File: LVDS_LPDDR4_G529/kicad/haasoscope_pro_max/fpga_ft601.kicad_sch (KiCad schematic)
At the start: 2 parts, among them U2 FT601Q_Aligned, U3 Ti90G529_Functions

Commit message: Aligned schematics, sort of
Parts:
- U3: footprint G529:BGA-529_23x23_19.0x19.0mm -> haasoscope_pro_adc_fpga_board:BGA-529_23x23_19.0x19.0mm
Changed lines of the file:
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@@
 			)
 		)
-		(property "Footprint" "G529:BGA-529_23x23_19.0x19.0mm"
+		(property "Footprint" "haasoscope_pro_adc_fpga_board:BGA-529_23x23_19.0x19.0mm"
 			(at 96.52 91.44 0)
 			(effects

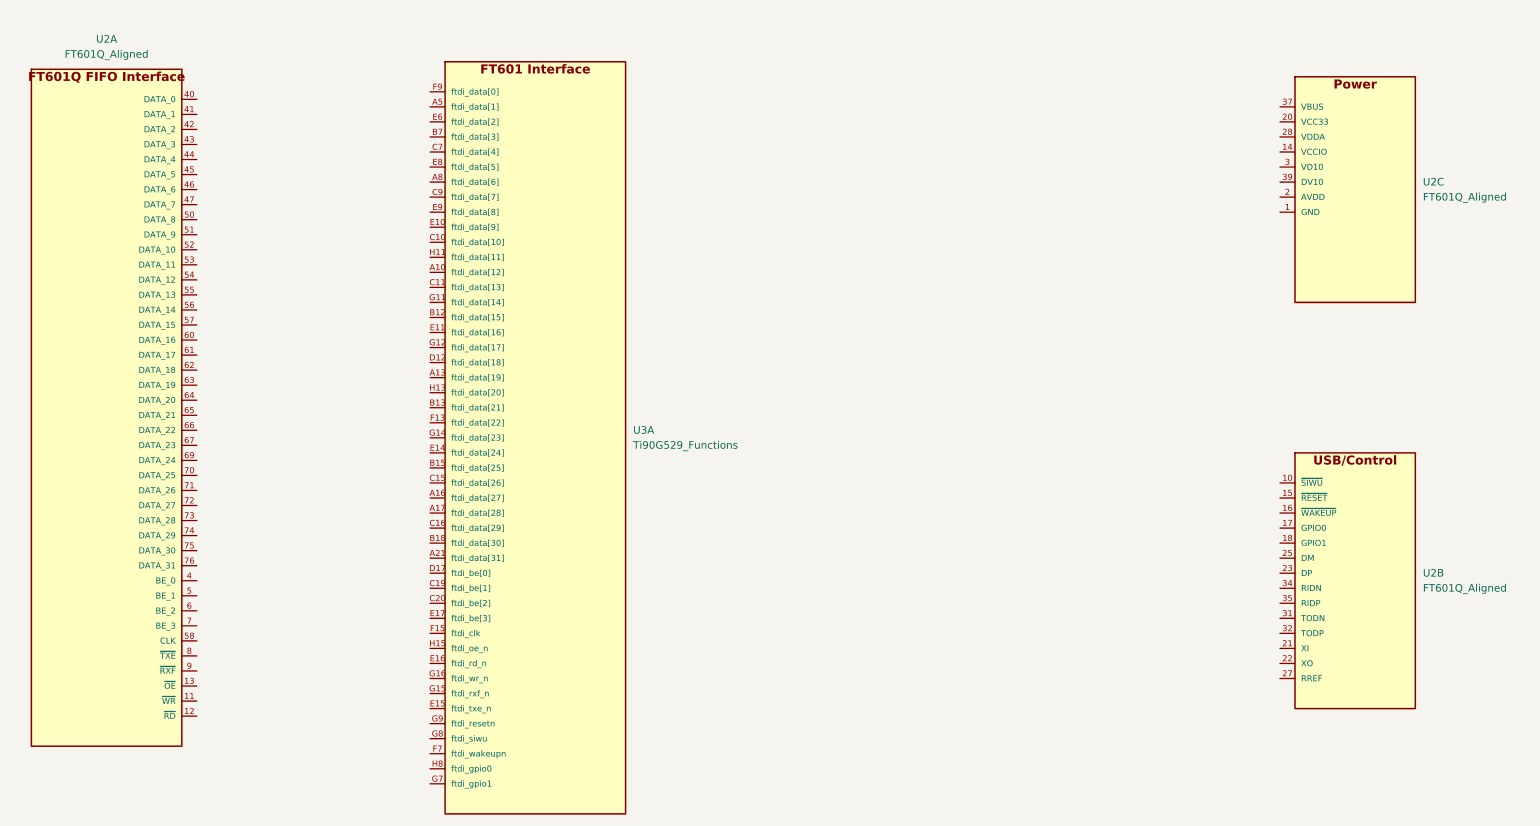
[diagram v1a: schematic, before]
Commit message: Aligned schematics, better
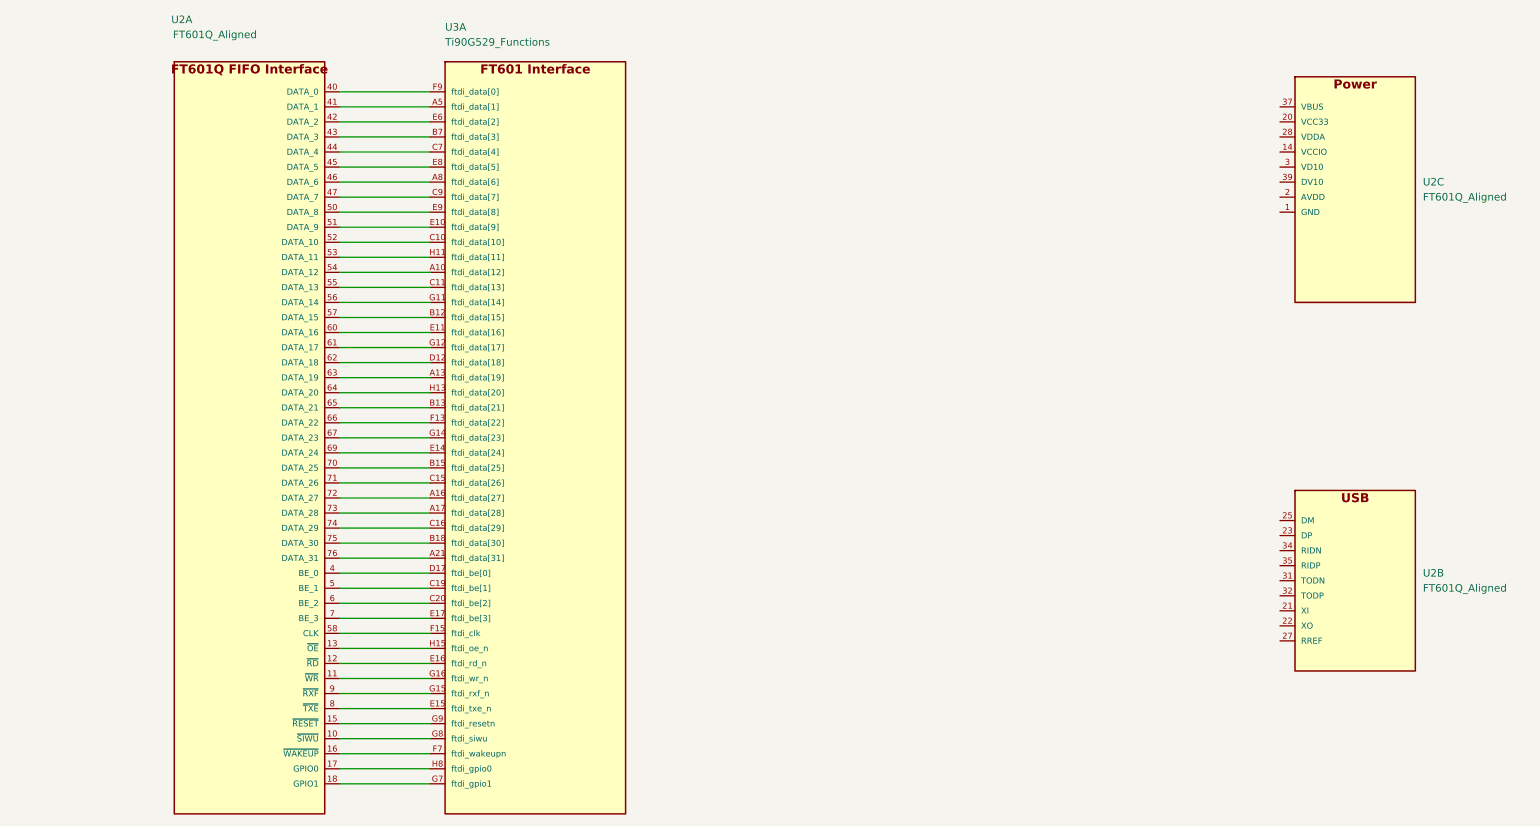
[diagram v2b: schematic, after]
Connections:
- net at U2.11 (~{WR}): now also U3.G16 (ftdi_wr_n)
- net at U2.12 (~{RD}): now also U3.E16 (ftdi_rd_n)
- net at U2.13 (~{OE}): now also U3.H15 (ftdi_oe_n)
- net at U2.4 (BE_0): now also U3.D17 (ftdi_be[0])
- net at U2.40 (DATA_0): now also U3.F9 (ftdi_data[0])
- net at U2.41 (DATA_1): now also U3.A5 (ftdi_data[1])
- net at U2.42 (DATA_2): now also U3.E6 (ftdi_data[2])
- net at U2.43 (DATA_3): now also U3.B7 (ftdi_data[3])
- net at U2.44 (DATA_4): now also U3.C7 (ftdi_data[4])
- net at U2.45 (DATA_5): now also U3.E8 (ftdi_data[5])
- net at U2.46 (DATA_6): now also U3.A8 (ftdi_data[6])
- net at U2.47 (DATA_7): now also U3.C9 (ftdi_data[7])
- net at U2.5 (BE_1): now also U3.C19 (ftdi_be[1])
- net at U2.50 (DATA_8): now also U3.E9 (ftdi_data[8])
- net at U2.51 (DATA_9): now also U3.E10 (ftdi_data[9])
- net at U2.52 (DATA_10): now also U3.C10 (ftdi_data[10])
- net at U2.53 (DATA_11): now also U3.H11 (ftdi_data[11])
- net at U2.54 (DATA_12): now also U3.A10 (ftdi_data[12])
- net at U2.55 (DATA_13): now also U3.C11 (ftdi_data[13])
- net at U2.56 (DATA_14): now also U3.G11 (ftdi_data[14])
- net at U2.57 (DATA_15): now also U3.B12 (ftdi_data[15])
- net at U2.58 (CLK): now also U3.F15 (ftdi_clk)
- net at U2.6 (BE_2): now also U3.C20 (ftdi_be[2])
- net at U2.60 (DATA_16): now also U3.E11 (ftdi_data[16])
- net at U2.61 (DATA_17): now also U3.G12 (ftdi_data[17])
- net at U2.62 (DATA_18): now also U3.D12 (ftdi_data[18])
- net at U2.63 (DATA_19): now also U3.A13 (ftdi_data[19])
- net at U2.64 (DATA_20): now also U3.H13 (ftdi_data[20])
- net at U2.65 (DATA_21): now also U3.B13 (ftdi_data[21])
- net at U2.66 (DATA_22): now also U3.F13 (ftdi_data[22])
- net at U2.67 (DATA_23): now also U3.G14 (ftdi_data[23])
- net at U2.69 (DATA_24): now also U3.E14 (ftdi_data[24])
- net at U2.7 (BE_3): now also U3.E17 (ftdi_be[3])
- net at U2.70 (DATA_25): now also U3.B15 (ftdi_data[25])
- net at U2.71 (DATA_26): now also U3.C15 (ftdi_data[26])
- net at U2.72 (DATA_27): now also U3.A16 (ftdi_data[27])
- net at U2.73 (DATA_28): now also U3.A17 (ftdi_data[28])
- net at U2.74 (DATA_29): now also U3.C16 (ftdi_data[29])
- net at U2.75 (DATA_30): now also U3.B18 (ftdi_data[30])
- net at U2.76 (DATA_31): now also U3.A21 (ftdi_data[31])
- net at U2.8 (~{TXE}): now also U3.E15 (ftdi_txe_n)
- net at U2.9 (~{RXF}): now also U3.G15 (ftdi_rxf_n)
- net at U3.F7 (ftdi_wakeupn): now also U2.16 (~{WAKEUP})
- net at U3.G7 (ftdi_gpio1): now also U2.18 (GPIO1)
- net at U3.G8 (ftdi_siwu): now also U2.10 (~{SIWU})
- net at U3.G9 (ftdi_resetn): now also U2.15 (~{RESET})
- net at U3.H8 (ftdi_gpio0): now also U2.17 (GPIO0)

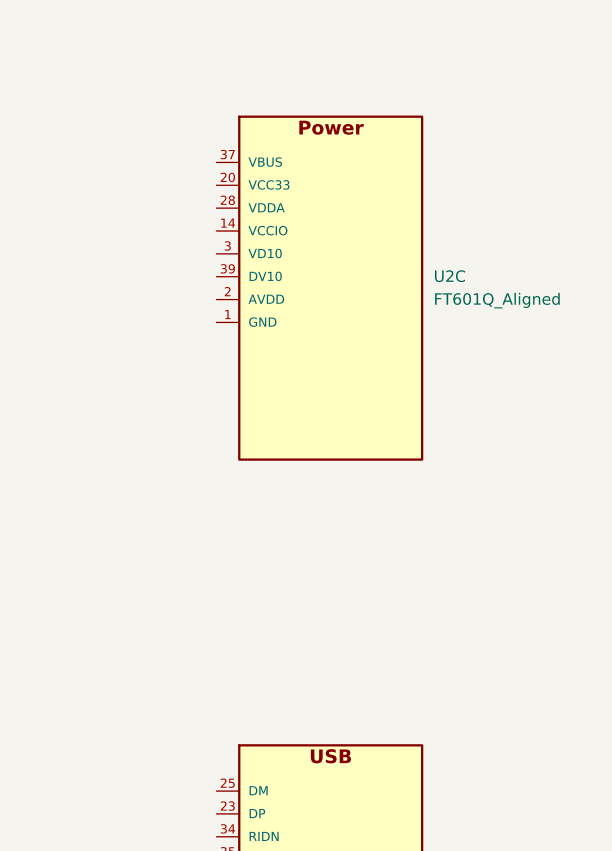
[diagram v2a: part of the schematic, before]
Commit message: Aligned schematics, connected some components
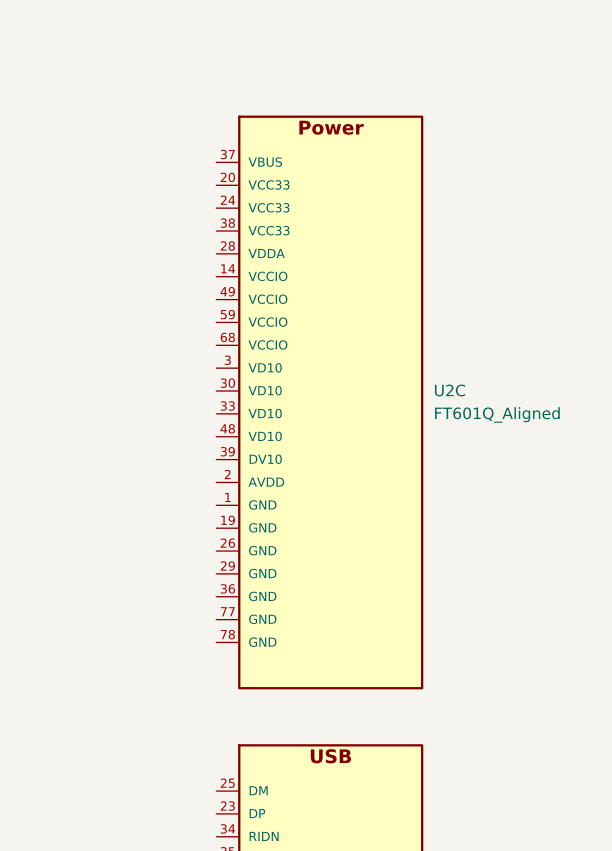
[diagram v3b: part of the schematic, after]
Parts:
- U3: footprint haasoscope_pro_adc_fpga_board:BGA-529_23x23_19.0x19.0mm -> G529:BGA-529_23x23_19.0x19.0mm
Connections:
- now unconnected: U2.24 (VCC33), U2.26 (GND), U2.28 (VDDA), U2.29 (GND), U2.3 (VD10), U2.30 (VD10), U2.33 (VD10), U2.36 (GND), U2.38 (VCC33), U2.39 (DV10), U2.48 (VD10), U2.49 (VCCIO), U2.59 (VCCIO), U2.68 (VCCIO), U2.77 (GND)
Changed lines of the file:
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@@
 		(pin "26"
+		)
+		(pin "19"
+		)
+		(pin "78"
 		)
 		(instances
@@
 		(pin "26"
 		)
+		(pin "19"
+		)
+		(pin "78"
+		)
 		(instances
 			(project ""
@@
 			)
 		)
-		(property "Footprint" "haasoscope_pro_adc_fpga_board:BGA-529_23x23_19.0x19.0mm"
+		(property "Footprint" "G529:BGA-529_23x23_19.0x19.0mm"
 			(at 96.52 91.44 0)
 			(effects
@@
 	(symbol
 		(lib_id "Aligned_Peripheral_Symbols:FT601Q_Aligned")
-		(at 240.03 45.72 0)
+		(at 240.03 58.42 0)
 		(unit 3)
 		(exclude_from_sim no)
@@
 		(fields_autoplaced yes)
 		(property "Reference" "U2"
-			(at 261.62 44.4352 0)
+			(at 261.62 57.1352 0)
 			(effects
 				(font
@@
 		)
 		(property "Value" "FT601Q_Aligned"
-			(at 261.62 46.9752 0)
+			(at 261.62 59.6752 0)
 			(effects
 				(font
@@
 		)
 		(property "Footprint" "Package_DFN_QFN:QFN-76-1EP_9x9mm_P0.4mm_EP5.81x6.31mm"
-			(at 240.03 49.53 0)
+			(at 240.03 62.23 0)
 			(effects
 				(font
@@
 		)
 		(property "Datasheet" ""
-			(at 240.03 45.72 0)
+			(at 240.03 58.42 0)
 			(effects
 				(font
@@
 		)
 		(property "Description" "FT601Q USB3 FIFO - pin ordering aligned with Ti90G529 FPGA"
-			(at 240.03 52.07 0)
+			(at 240.03 64.77 0)
 			(effects
 				(font
@@
 		(pin "26"
 		)
+		(pin "19"
+		)
+		(pin "78"
+		)
 		(instances

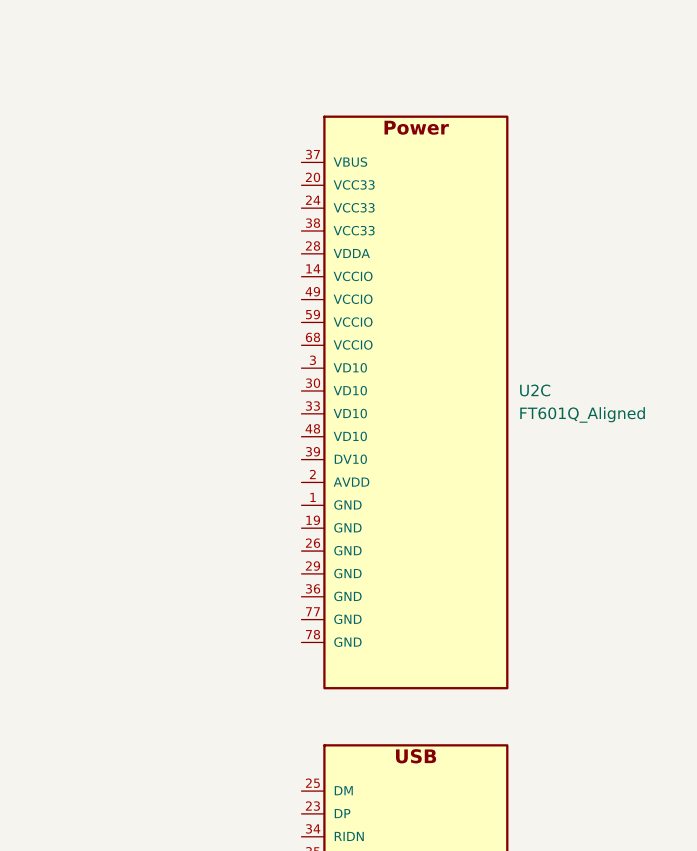
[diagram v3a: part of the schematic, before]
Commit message: an lvds routed
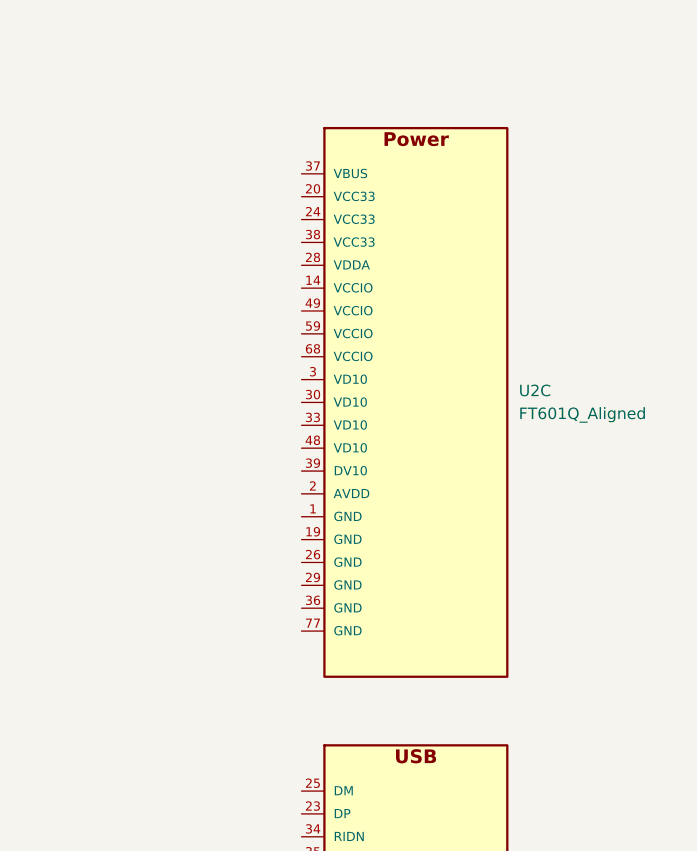
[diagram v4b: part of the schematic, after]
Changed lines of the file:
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@@
 	)
 	(symbol
+		(lib_name "FT601Q_Aligned_1")
 		(lib_id "Aligned_Peripheral_Symbols:FT601Q_Aligned")
 		(at 240.03 58.42 0)
@@
 		(pin "19"
 		)
-		(pin "78"
-		)
 		(instances
